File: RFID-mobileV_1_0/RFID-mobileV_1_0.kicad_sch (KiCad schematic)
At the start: 36 parts

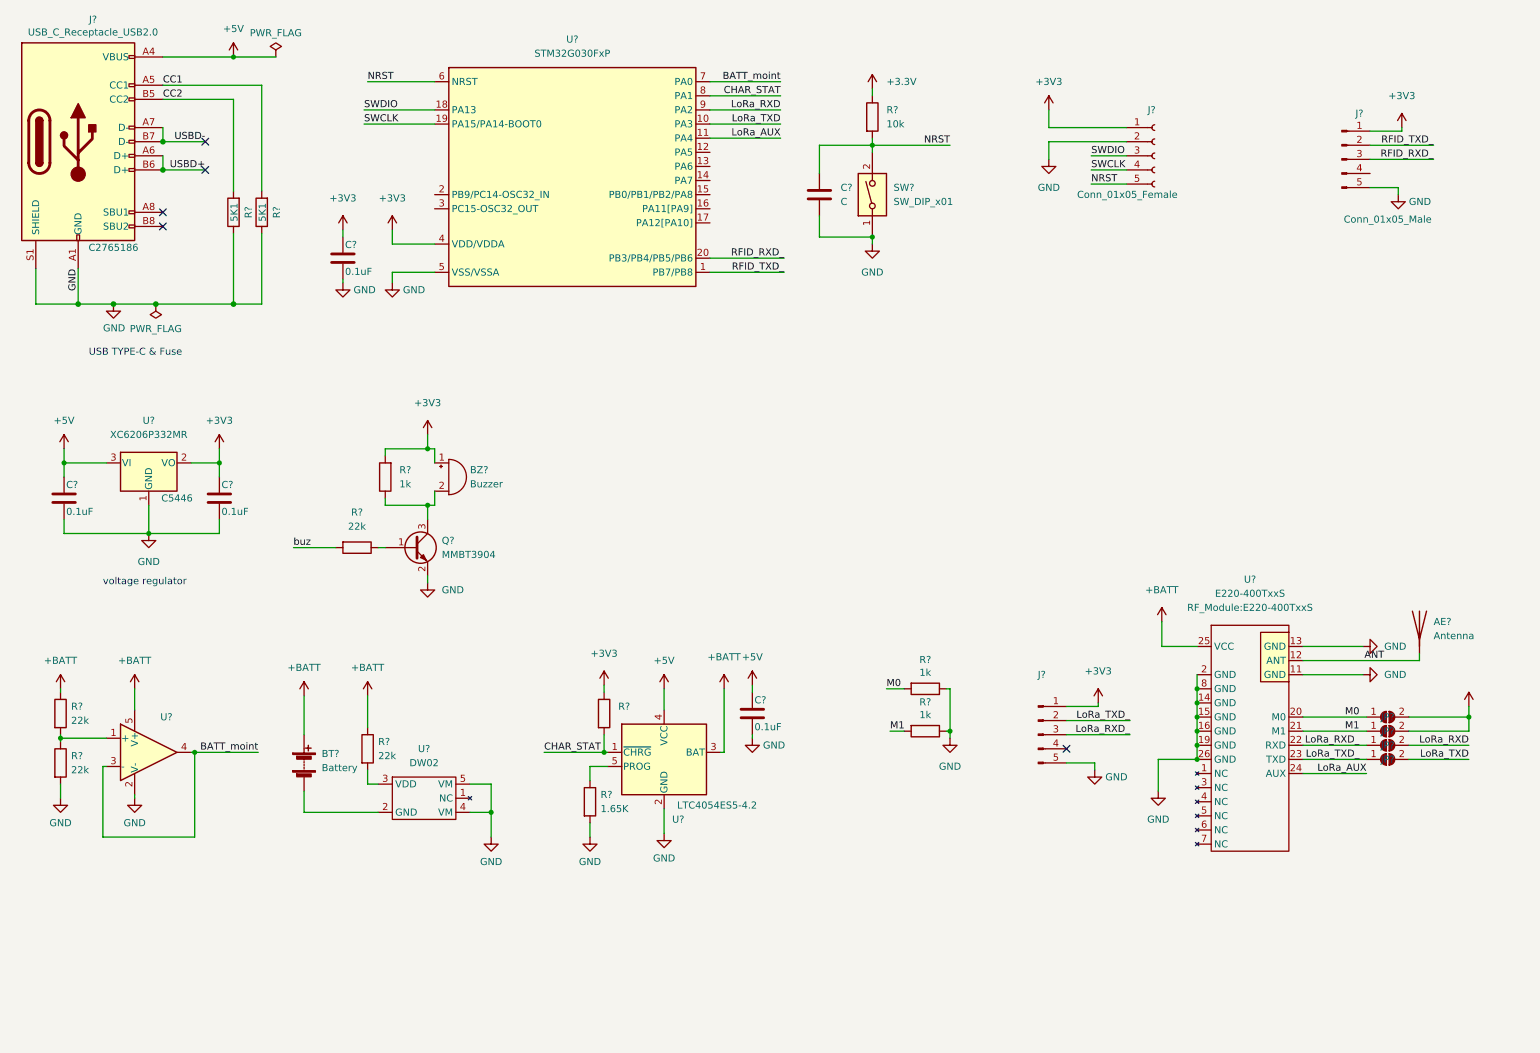
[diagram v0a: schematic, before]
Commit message: add board edge
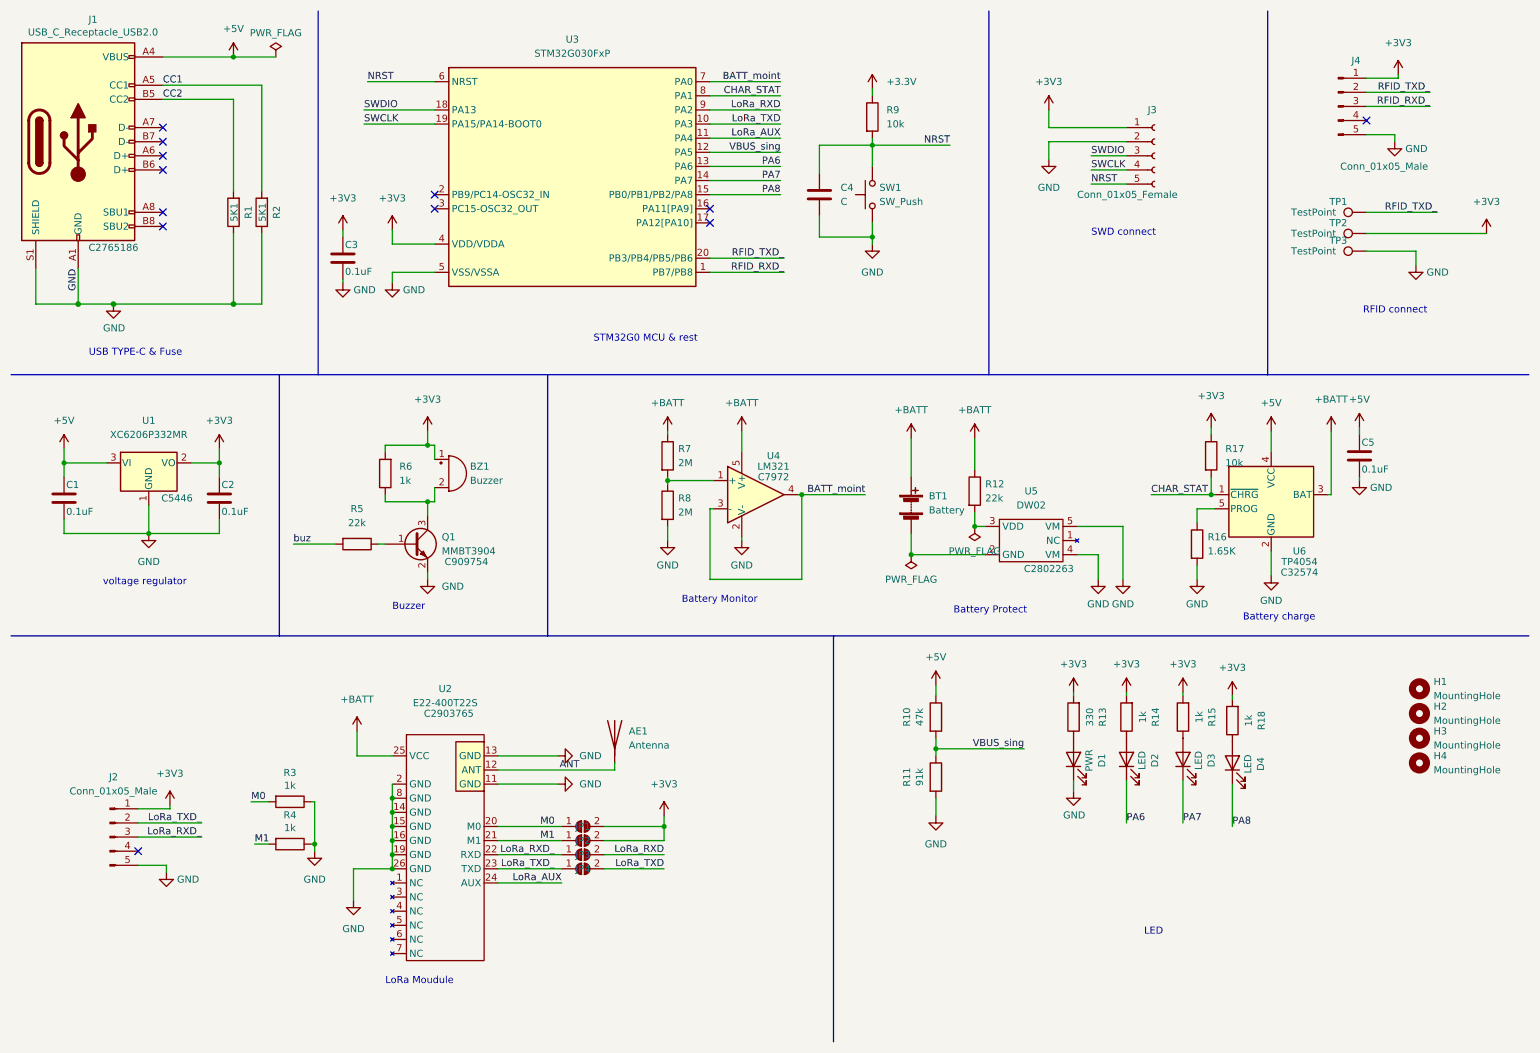
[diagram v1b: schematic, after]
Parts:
- removed SW?: SW_DIP_x01, Button_Switch_SMD:SW_DIP_SPSTx01_Slide_6.7x4.1mm_W8.61mm_P2.54mm_LowProfile, symbol Switch:SW_DIP_x01
- added D1: PWR, LED_SMD:LED_0805_2012Metric, symbol Device:LED
- added D2, D3, D4: LED, LED_SMD:LED_0805_2012Metric, symbol Device:LED
- added H1, H2, H3, H4: MountingHole, MountingHole:MountingHole_3.2mm_M3, symbol Mechanical:MountingHole
- added R10: 47k, Resistor_SMD:R_0805_2012Metric, symbol Device:R
- added R11: 91k, Resistor_SMD:R_0805_2012Metric, symbol Device:R
- added R13: 330, Resistor_SMD:R_0805_2012Metric, symbol Device:R
- added R14, R15, R18: 1k, Resistor_SMD:R_0805_2012Metric, symbol Device:R
- added SW1: SW_Push, Button_Switch_SMD:SW_SPST_TL3305A, symbol Switch:SW_Push
- added TP1, TP2, TP3: TestPoint, TestPoint:TestPoint_Pad_1.5x1.5mm, symbol Connector:TestPoint
- BT1: renamed from BT?; footprint (none) -> Connector_Molex:Molex_KK-254_AE-6410-02A_1x02_P2.54mm_Vertical
- BZ1: renamed from BZ?; LCSC (none) -> C113159; LCSC Part# C113159 -> (none)
- C4: renamed from C?; footprint (none) -> Capacitor_SMD:C_0805_2012Metric
- J2: renamed from J?; value (none) -> Conn_01x05_Male; footprint (none) -> Connector_PinHeader_2.54mm:PinHeader_1x05_P2.54mm_Vertical
- JP1, JP2: renamed from JP?; footprint (none) -> Jumper:SolderJumper-2_P1.3mm_Open_RoundedPad1.0x1.5mm
- JP3, JP4: renamed from JP?; value (none) -> SolderJumper_2_Open; footprint (none) -> Jumper:SolderJumper-2_P1.3mm_Open_RoundedPad1.0x1.5mm
- Q1: renamed from Q?; LCSC (none) -> C909754
- R17: renamed from R?; value (none) -> 10k; footprint (none) -> Resistor_SMD:R_0805_2012Metric
- R7, R8: renamed from R?; value 22k -> 2M
- U2: renamed from U?; value E220-400TxxS -> E22-400T22S; LCSC (none) -> C2903765
- U3: renamed from U?; LCSC (none) -> C529330
- U4: renamed from U?; value (none) -> LM321; footprint (none) -> Package_TO_SOT_SMD:SOT-23-5
- U6: renamed from U?; value LTC4054ES5-4.2 -> TP4054
- gave numbers to parts that had none: 19
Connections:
- net +3V3: now also R13.2, R14.2, R15.2, R18.2, TP2.1
- net +5V: now also R10.1
- net GND: now also D1.1 (K), R11.2, SW1.1, TP3.1
- net NRST: now also SW1.2
- net RFID_RXD_: now also U3.1 (PB7/PB8); no longer U3.20 (PB3/PB4/PB5/PB6)
- net RFID_TXD_: now also U3.20 (PB3/PB4/PB5/PB6), TP1.1; no longer U3.1 (PB7/PB8)
- net VBUS_sing: now reaches U3.12 (PA5)
- net VBUS_sing: now also R10.2, R11.1
- net PA6: now reaches U3.13 (PA6)
- net PA6: now also D2.1 (K)
- net PA7: now reaches U3.14 (PA7)
- net PA7: now also D3.1 (K)
- net PA8: now reaches U3.15 (PB0/PB1/PB2/PA8)
- net PA8: now also D4.1 (K)
- net USBD+: no longer names the net of J1.A6 (D+)
- net USBD+: no longer J1.B6 (D+)
- net USBD-: no longer names the net of J1.A7 (D-)
- net USBD-: no longer J1.B7 (D-)
- new net: D4.2 (A), R18.1
- new net: D2.2 (A), R14.1
- new net: D3.2 (A), R15.1
- new net: D1.2 (A), R13.1
- no-connect marks 5 -> 12
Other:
- note added: "Battery Monitor"
- note added: "Battery Protect"
- note added: "Battery charge"
- note added: "Buzzer"
- note added: "LED"
- note added: "LoRa Moudule"
- note added: "RFID connect"
- note added: "STM32G0 MCU & rest"
- note added: "SWD connect"
- moved on the sheet: AE1, BT1, BZ1, C5, J2, J4, JP1, JP2, JP3, JP4, Q1, R12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

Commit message: add
PCB Broad edge
place Device
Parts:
- added C6: 0.1uF, Capacitor_SMD:C_0805_2012Metric, symbol Device:C
- J3: value Conn_01x05_Female -> (none); footprint Connector_Harwin:Harwin_M20-89005xx_1x05_P2.54mm_Horizontal -> (none)
- JP1, JP2, JP3, JP4: value SolderJumper_2_Open -> (none); footprint Jumper:SolderJumper-2_P1.3mm_Open_RoundedPad1.0x1.5mm -> (none); now left out of the parts list
- TP1: value TestPoint -> (none); footprint TestPoint:TestPoint_Pad_1.5x1.5mm -> (none)
- TP2, TP3: value TestPoint -> (none)
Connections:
- net +BATT: now also C6.1
- net GND: now also C6.2
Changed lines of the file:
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@@
+    (stroke (width 0) (type default) (color 0 0 0 0))
+  )
+  (wire (pts (xy 120.65 87.63) (xy 120.65 89.535))
     (stroke (width 0) (type default) (color 0 0 0 0))
   )
@@
   )
   (wire (pts (xy 75.565 32.385) (xy 88.265 32.385))
+    (stroke (width 0) (type default) (color 0 0 0 0))
+  )
+  (wire (pts (xy 120.65 97.155) (xy 120.65 107.315))
     (stroke (width 0) (type default) (color 0 0 0 0))
   )
@@
     (in_bom no) (on_board yes)
     (property "Reference" "TP3" (id 0) (at 250.825 53.34 90))
-    (property "Value" "TestPoint" (id 1) (at 246.38 55.245 90))
+    (property "Value" "" (id 1) (at 246.38 55.245 90))
     (property "Footprint" "TestPoint:TestPoint_Pad_1.5x1.5mm" (id 2) (at 255.905 50.165 0)
       (effects (font (size 1.27 1.27)) hide)
@@
     (pin "1")
     (pin "2")
+  )
+  (symbol (lib_id "power:+BATT") (at 120.65 87.63 0) (unit 1)
+    (in_bom yes) (on_board yes) (fields_autoplaced)
+    (property "Reference" "#PWR050" (id 0) (at 120.65 91.44 0)
+      (effects (font (size 1.27 1.27)) hide)
+    )
+    (property "Value" "+BATT" (id 1) (at 120.65 82.55 0))
+    (property "Footprint" "" (id 2) (at 120.65 87.63 0)
+      (effects (font (size 1.27 1.27)) hide)
+    )
+    (property "Datasheet" "" (id 3) (at 120.65 87.63 0)
+      (effects (font (size 1.27 1.27)) hide)
+    )
+    (pin "1")
   )
   (symbol (lib_id "Device:R") (at 62.23 161.925 270) (unit 1)
@@
     (in_bom no) (on_board yes)
     (property "Reference" "TP1" (id 0) (at 250.825 46.355 90))
-    (property "Value" "TestPoint" (id 1) (at 246.38 48.26 90))
-    (property "Footprint" "TestPoint:TestPoint_Pad_1.5x1.5mm" (id 2) (at 255.905 43.18 0)
+    (property "Value" "" (id 1) (at 246.38 48.26 90))
+    (property "Footprint" "" (id 2) (at 255.905 43.18 0)
       (effects (font (size 1.27 1.27)) hide)
     )
@@
     (pin "1")
   )
+  (symbol (lib_id "Device:C") (at 120.65 93.345 0) (unit 1)
+    (in_bom yes) (on_board yes)
+    (property "Reference" "C6" (id 0) (at 121.031 90.926 0)
+      (effects (font (size 1.27 1.27)) (justify left))
+    )
+    (property "Value" "0.1uF" (id 1) (at 121.031 95.764 0)
+      (effects (font (size 1.27 1.27)) (justify left))
+    )
+    (property "Footprint" "Capacitor_SMD:C_0805_2012Metric" (id 2) (at 121.6152 97.155 0)
+      (effects (font (size 1.27 1.27)) hide)
+    )
+    (property "Datasheet" "~" (id 3) (at 120.65 93.345 0)
+      (effects (font (size 1.27 1.27)) hide)
+    )
+    (property "LCSC" "C49678" (id 4) (at 120.65 93.345 0)
+      (effects (font (size 1.27 1.27)) hide)
+    )
+    (pin "1")
+    (pin "2")
+  )
   (symbol (lib_id "power:PWR_FLAG") (at 185.42 104.775 180) (unit 1)
     (in_bom yes) (on_board yes)
@@
   )
   (symbol (lib_id "Jumper:SolderJumper_2_Open") (at 114.935 166.37 0) (unit 1)
-    (in_bom yes) (on_board yes)
-    (property "Reference" "JP4" (id 0) (at 114.935 166.37 0))
-    (property "Value" "SolderJumper_2_Open" (id 1) (at 125.095 168.275 0)
-      (effects (font (size 1.27 1.27)) hide)
-    )
-    (property "Footprint" "Jumper:SolderJumper-2_P1.3mm_Open_RoundedPad1.0x1.5mm" (id 2) (at 114.935 166.37 0)
+    (in_bom no) (on_board yes)
+    (property "Reference" "JP4" (id 0) (at 116.84 165.1 0))
+    (property "Value" "" (id 1) (at 125.095 168.275 0)
+      (effects (font (size 1.27 1.27)) hide)
+    )
+    (property "Footprint" "" (id 2) (at 114.935 166.37 0)
       (effects (font (size 1.27 1.27)) hide)
     )
@@
     (in_bom no) (on_board yes)
     (property "Reference" "TP2" (id 0) (at 250.825 50.165 90))
-    (property "Value" "TestPoint" (id 1) (at 246.38 52.07 90))
+    (property "Value" "" (id 1) (at 246.38 52.07 90))
     (property "Footprint" "TestPoint:TestPoint_Pad_1.5x1.5mm" (id 2) (at 255.905 46.99 0)
       (effects (font (size 1.27 1.27)) hide)
@@
   )
   (symbol (lib_id "Jumper:SolderJumper_2_Open") (at 114.935 161.29 0) (unit 1)
-    (in_bom yes) (on_board yes)
-    (property "Reference" "JP2" (id 0) (at 114.935 161.29 0))
-    (property "Value" "SolderJumper_2_Open" (id 1) (at 125.095 163.195 0)
-      (effects (font (size 1.27 1.27)) hide)
-    )
-    (property "Footprint" "Jumper:SolderJumper-2_P1.3mm_Open_RoundedPad1.0x1.5mm" (id 2) (at 114.935 161.29 0)
+    (in_bom no) (on_board yes)
+    (property "Reference" "JP2" (id 0) (at 116.84 160.02 0))
+    (property "Value" "" (id 1) (at 125.095 163.195 0)
+      (effects (font (size 1.27 1.27)) hide)
+    )
+    (property "Footprint" "" (id 2) (at 114.935 161.29 0)
       (effects (font (size 1.27 1.27)) hide)
     )
@@
       (effects (font (size 1.27 1.27)) (justify left))
     )
-    (property "Value" "Conn_01x05_Female" (id 1) (at 203.835 45.085 0)
-      (effects (font (size 1.27 1.27)) (justify left))
-    )
-    (property "Footprint" "Connector_Harwin:Harwin_M20-89005xx_1x05_P2.54mm_Horizontal" (id 2) (at 217.805 38.1 0)
+    (property "Value" "" (id 1) (at 203.835 45.085 0)
+      (effects (font (size 1.27 1.27)) (justify left))
+    )
+    (property "Footprint" "" (id 2) (at 217.805 38.1 0)
       (effects (font (size 1.27 1.27)) hide)
     )
@@
   )
   (symbol (lib_id "Jumper:SolderJumper_2_Open") (at 114.935 158.75 0) (unit 1)
-    (in_bom yes) (on_board yes)
-    (property "Reference" "JP1" (id 0) (at 114.935 158.75 0))
-    (property "Value" "SolderJumper_2_Open" (id 1) (at 125.095 160.655 0)
-      (effects (font (size 1.27 1.27)) hide)
-    )
-    (property "Footprint" "Jumper:SolderJumper-2_P1.3mm_Open_RoundedPad1.0x1.5mm" (id 2) (at 114.935 158.75 0)
+    (in_bom no) (on_board yes)
+    (property "Reference" "JP1" (id 0) (at 116.84 157.48 0))
+    (property "Value" "" (id 1) (at 125.095 160.655 0)
+      (effects (font (size 1.27 1.27)) hide)
+    )
+    (property "Footprint" "" (id 2) (at 114.935 158.75 0)
       (effects (font (size 1.27 1.27)) hide)
     )
@@
     (pin "2")
   )
+  (symbol (lib_id "power:GND") (at 120.65 107.315 0) (unit 1)
+    (in_bom yes) (on_board yes) (fields_autoplaced)
+    (property "Reference" "#PWR051" (id 0) (at 120.65 113.665 0)
+      (effects (font (size 1.27 1.27)) hide)
+    )
+    (property "Value" "GND" (id 1) (at 120.65 111.76 0))
+    (property "Footprint" "" (id 2) (at 120.65 107.315 0)
+      (effects (font (size 1.27 1.27)) hide)
+    )
+    (property "Datasheet" "" (id 3) (at 120.65 107.315 0)
+      (effects (font (size 1.27 1.27)) hide)
+    )
+    (pin "1")
+  )
   (symbol (lib_id "Device:R") (at 203.2 139.065 180) (unit 1)
     (in_bom yes) (on_board yes)
@@
   )
   (symbol (lib_id "Jumper:SolderJumper_2_Open") (at 114.935 163.83 0) (unit 1)
-    (in_bom yes) (on_board yes)
-    (property "Reference" "JP3" (id 0) (at 114.935 163.83 0))
-    (property "Value" "SolderJumper_2_Open" (id 1) (at 125.73 161.925 0)
-      (effects (font (size 1.27 1.27)) hide)
-    )
-    (property "Footprint" "Jumper:SolderJumper-2_P1.3mm_Open_RoundedPad1.0x1.5mm" (id 2) (at 114.935 163.83 0)
+    (in_bom no) (on_board yes)
+    (property "Reference" "JP3" (id 0) (at 116.84 162.56 0))
+    (property "Value" "" (id 1) (at 125.73 161.925 0)
+      (effects (font (size 1.27 1.27)) hide)
+    )
+    (property "Footprint" "" (id 2) (at 114.935 163.83 0)
       (effects (font (size 1.27 1.27)) hide)
     )
@@
       (reference "#PWR049") (unit 1) (value "+3V3") (footprint "")
     )
+    (path "/0ba4cdad-4e4c-4a66-a720-4a84e6dd729f"
+      (reference "#PWR050") (unit 1) (value "+BATT") (footprint "")
+    )
+    (path "/ebbbfacc-2ba2-46ee-a426-7436393bbbcc"
+      (reference "#PWR051") (unit 1) (value "GND") (footprint "")
+    )
     (path "/ac27cb01-7e08-4126-9053-c19587e4f0b6"
       (reference "AE1") (unit 1) (value "Antenna") (footprint "RF_Antenna:433MHz")
@@
       (reference "C5") (unit 1) (value "0.1uF") (footprint "Capacitor_SMD:C_0805_2012Metric")
     )
+    (path "/953f90df-a503-4127-807f-9782c4499e61"
+      (reference "C6") (unit 1) (value "0.1uF") (footprint "Capacitor_SMD:C_0805_2012Metric")
+    )
     (path "/d727a027-5130-4f66-84b9-1203310f2112"
       (reference "D1") (unit 1) (value "PWR") (footprint "LED_SMD:LED_0805_2012Metric")
@@
     )
     (path "/b6456f58-6f7c-4f47-87b0-12c2581b9317"
-      (reference "J3") (unit 1) (value "Conn_01x05_Female") (footprint "Connector_Harwin:Harwin_M20-89005xx_1x05_P2.54mm_Horizontal")
+      (reference "J3") (unit 1) (value "Conn_01x05_Female") (footprint "Connector_PinHeader_2.54mm:PinHeader_1x05_P2.54mm_Vertical")
     )
     (path "/3a6044fd-f2c2-47bf-abb4-e3181c44ba68"
@@
     )
     (path "/5b5af4a2-eb2c-4530-90d8-d7a1b678f6fa"
-      (reference "TP1") (unit 1) (value "TestPoint") (footprint "TestPoint:TestPoint_Pad_1.5x1.5mm")
+      (reference "TP1") (unit 1) (value "RFID_TX") (footprint "TestPoint:TestPoint_Pad_1.5x1.5mm")
     )
     (path "/a1418178-3803-4904-8ab9-1d954a912710"
-      (reference "TP2") (unit 1) (value "TestPoint") (footprint "TestPoint:TestPoint_Pad_1.5x1.5mm")
+      (reference "TP2") (unit 1) (value "3.3V") (footprint "TestPoint:TestPoint_Pad_1.5x1.5mm")
     )
     (path "/029b884c-da32-436d-8710-4e4d9ed39def"
-      (reference "TP3") (unit 1) (value "TestPoint") (footprint "TestPoint:TestPoint_Pad_1.5x1.5mm")
+      (reference "TP3") (unit 1) (value "GND") (footprint "TestPoint:TestPoint_Pad_1.5x1.5mm")
     )
     (path "/911aa946-11a4-4082-a79a-bc4f1c265350"
